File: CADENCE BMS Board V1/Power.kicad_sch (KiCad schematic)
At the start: 62 parts, among them J20 Conn_01x02, J28 Banana Socket PWR, J29 Banana Socket VSS, U1 TVS2200DRV, U2 LT8612, U3 LT3652IMSE#PBF

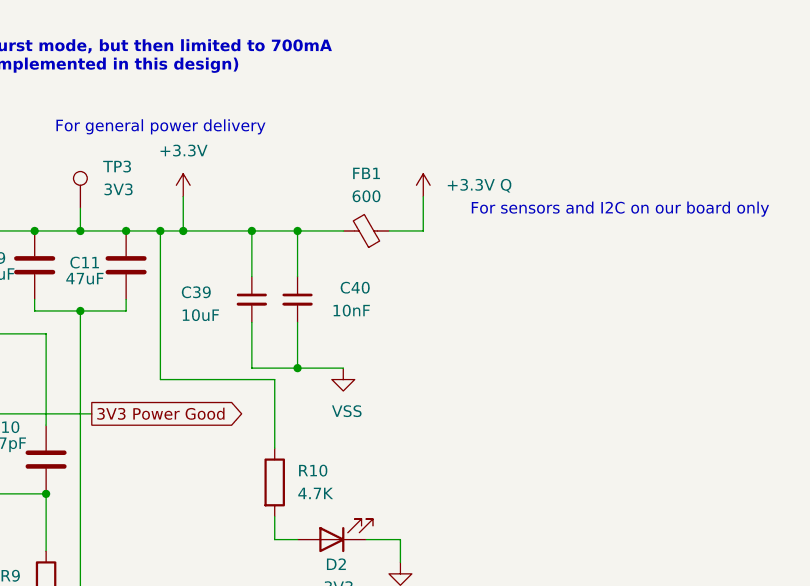
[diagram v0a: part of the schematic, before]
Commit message: Removed 3v3Q
Removed 3v3Q, Capacitors (EMI FILTER OUT), Changed all +3.3V Q -> 3.3V
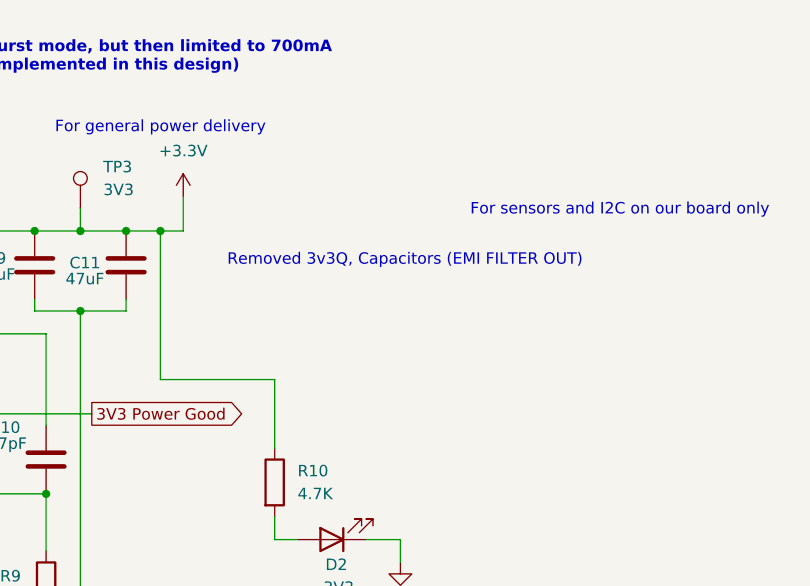
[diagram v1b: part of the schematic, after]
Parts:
- removed C39: 10uF, Capacitor_SMD:C_1210_3225Metric, symbol Device:C_Small
- removed C40: 10nF, Capacitor_SMD:C_0805_2012Metric, symbol Device:C_Small
- removed FB1: 600, Inductor_SMD:L_1008_2520Metric, symbol Device:FerriteBead_Small
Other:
- note added: "Removed 3v3Q, Capacitors (EMI FILTER OUT)"

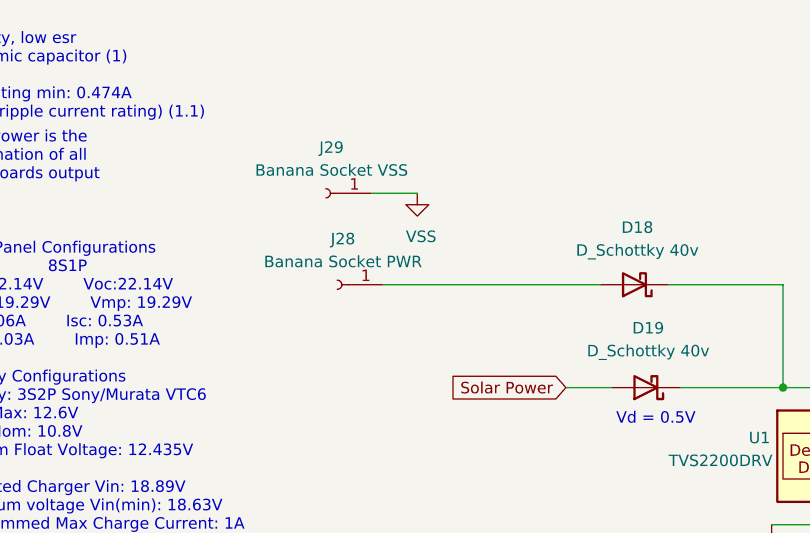
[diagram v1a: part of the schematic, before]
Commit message: Updates for USB-C charging and set up for testing
Revamped USB-C layout to make it cleaner and more compressed and also included schematic parts for adding in Banana plugs for testing the PCB
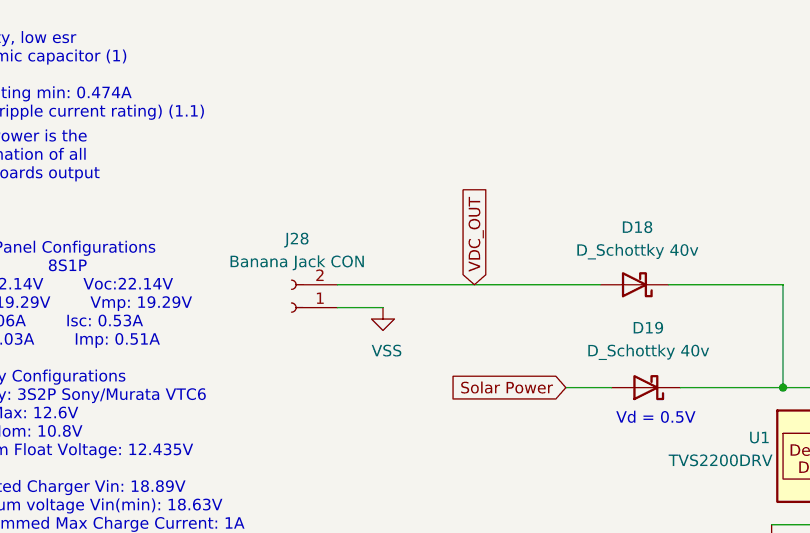
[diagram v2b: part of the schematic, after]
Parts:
- removed J28: Banana Socket PWR, Connector:Banana_Cliff_FCR7350R_S16N-PC_Horizontal, symbol Connector:Conn_01x01_Socket
- removed J29: Banana Socket VSS, Connector:Banana_Cliff_FCR7350B_S16N-PC_Horizontal, symbol Connector:Conn_01x01_Socket
- added J28: Banana Jack CON, Connector:Banana_Jack_2Pin, symbol Connector:Conn_01x02_Socket
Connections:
- net VSS: now also J28.1 (Pin_1)
- net VDC_OUT: now reaches D18.2 (A)
- net VDC_OUT: now also J28.2 (Pin_2)
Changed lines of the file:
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@@
 	(wire
 		(pts
-			(xy 78.74 46.99) (xy 102.87 46.99)
-		)
-		(stroke
-			(width 0)
-			(type default)
-		)
-	)
-	(wire
-		(pts
 			(xy 124.46 331.47) (xy 124.46 337.82)
 		)
@@
 	(wire
 		(pts
-			(xy 77.47 36.83) (xy 82.55 36.83)
+			(xy 73.66 49.53) (xy 78.74 49.53)
 		)
 		(stroke
@@
 	(wire
 		(pts
+			(xy 73.66 46.99) (xy 102.87 46.99)
+		)
+		(stroke
+			(width 0)
+			(type default)
+		)
+	)
+	(wire
+		(pts
 			(xy 341.63 63.5) (xy 346.71 63.5)
 		)
@@
 		)
 	)
+	(global_label "VDC_OUT"
+		(shape input)
+		(at 88.9 46.99 90)
+		(fields_autoplaced yes)
+		(effects
+			(font
+				(size 1.27 1.27)
+			)
+			(justify left)
+		)
+		(property "Intersheetrefs" "${INTERSHEET_REFS}"
+			(at 88.9 35.78 90)
+			(hide yes)
+			(show_name no)
+			(do_not_autoplace no)
+			(effects
+				(font
+					(size 1.27 1.27)
+				)
+				(justify left)
+			)
+		)
+	)
 	(global_label "NTC"
 		(shape input)
@@
 	)
 	(symbol
-		(lib_id "Connector:Conn_01x01_Socket")
-		(at 73.66 46.99 180)
-		(unit 1)
-		(body_style 1)
-		(exclude_from_sim no)
-		(in_bom yes)
-		(on_board yes)
-		(in_pos_files yes)
-		(dnp no)
-		(fields_autoplaced yes)
-		(property "Reference" "J28"
-			(at 74.295 41.91 0)
-			(show_name no)
-			(do_not_autoplace no)
-			(effects
-				(font
-					(size 1.27 1.27)
-				)
-			)
-		)
-		(property "Value" "Banana Socket PWR"
-			(at 74.295 44.45 0)
-			(show_name no)
-			(do_not_autoplace no)
-			(effects
-				(font
-					(size 1.27 1.27)
-				)
-			)
-		)
-		(property "Footprint" "Connector:Banana_Cliff_FCR7350R_S16N-PC_Horizontal"
-			(at 73.66 46.99 0)
-			(hide yes)
-			(show_name no)
-			(do_not_autoplace no)
-			(effects
-				(font
-					(size 1.27 1.27)
-				)
-			)
-		)
-		(property "Datasheet" ""
-			(at 73.66 46.99 0)
-			(hide yes)
-			(show_name no)
-			(do_not_autoplace no)
-			(effects
-				(font
-					(size 1.27 1.27)
-				)
-			)
-		)
-		(property "Description" "Generic connector, single row, 01x01, script generated"
-			(at 73.66 46.99 0)
-			(hide yes)
-			(show_name no)
-			(do_not_autoplace no)
-			(effects
-				(font
-					(size 1.27 1.27)
-				)
-			)
-		)
-		(pin "1"
-		)
-		(instances
-			(project "BMS_Board_Prototype"
-				(path "/4ee99911-836b-4752-8a2d-327c8b28dc47/f4fcff51-0cdb-4e70-aba0-d567fd3e6a03"
-					(reference "J28")
-					(unit 1)
-				)
-			)
-		)
-	)
-	(symbol
 		(lib_id "Device:C")
 		(at 341.63 71.12 0)
@@
 	(symbol
 		(lib_id "power:GND")
-		(at 82.55 36.83 0)
+		(at 78.74 49.53 0)
 		(unit 1)
 		(body_style 1)
@@
 		(dnp no)
 		(property "Reference" "#PWR033"
-			(at 82.55 43.18 0)
+			(at 78.74 55.88 0)
 			(hide yes)
 			(show_name no)
@@
 		)
 		(property "Value" "VSS"
-			(at 81.28 41.656 0)
+			(at 77.47 54.356 0)
 			(show_name no)
 			(do_not_autoplace no)
@@
 		)
 		(property "Footprint" ""
-			(at 82.55 36.83 0)
+			(at 78.74 49.53 0)
 			(hide yes)
 			(show_name no)
@@
 		)
 		(property "Datasheet" ""
-			(at 82.55 36.83 0)
+			(at 78.74 49.53 0)
 			(hide yes)
 			(show_name no)
@@
 		)
 		(property "Description" "Power symbol creates a global label with name \"GND\" , ground"
-			(at 82.55 36.83 0)
+			(at 78.74 49.53 0)
 			(hide yes)
 			(show_name no)
@@
 	)
 	(symbol
+		(lib_id "Connector:Conn_01x02_Socket")
+		(at 68.58 49.53 180)
+		(unit 1)
+		(body_style 1)
+		(exclude_from_sim no)
+		(in_bom yes)
+		(on_board yes)
+		(in_pos_files yes)
+		(dnp no)
+		(fields_autoplaced yes)
+		(property "Reference" "J28"
+			(at 69.215 41.91 0)
+			(show_name no)
+			(do_not_autoplace no)
+			(effects
+				(font
+					(size 1.27 1.27)
+				)
+			)
+		)
+		(property "Value" "Banana Jack CON"
+			(at 69.215 44.45 0)
+			(show_name no)
+			(do_not_autoplace no)
+			(effects
+				(font
+					(size 1.27 1.27)
+				)
+			)
+		)
+		(property "Footprint" "Connector:Banana_Jack_2Pin"
+			(at 68.58 49.53 0)
+			(hide yes)
+			(show_name no)
+			(do_not_autoplace no)
+			(effects
+				(font
+					(size 1.27 1.27)
+				)
+			)
+		)
+		(property "Datasheet" ""
+			(at 68.58 49.53 0)
+			(hide yes)
+			(show_name no)
+			(do_not_autoplace no)
+			(effects
+				(font
+					(size 1.27 1.27)
+				)
+			)
+		)
+		(property "Description" "Generic connector, single row, 01x02, script generated"
+			(at 68.58 49.53 0)
+			(hide yes)
+			(show_name no)
+			(do_not_autoplace no)
+			(effects
+				(font
+					(size 1.27 1.27)
+				)
+			)
+		)
+		(pin "1"
+		)
+		(pin "2"
+		)
+		(instances
+			(project "BMS_Board_Prototype"
+				(path "/4ee99911-836b-4752-8a2d-327c8b28dc47/f4fcff51-0cdb-4e70-aba0-d567fd3e6a03"
+					(reference "J28")
+					(unit 1)
+				)
+			)
+		)
+	)
+	(symbol
 		(lib_id "power:GND")
 		(at 88.9 327.66 0)
@@
 					(unit 1)
 				)
-			)
-		)
-	)
-	(symbol
-		(lib_id "Connector:Conn_01x01_Socket")
-		(at 72.39 36.83 180)
-		(unit 1)
-		(body_style 1)
-		(exclude_from_sim no)
-		(in_bom yes)
-		(on_board yes)
-		(in_pos_files yes)
-		(dnp no)
-		(fields_autoplaced yes)
-		(property "Reference" "J29"
-			(at 73.025 31.75 0)
-			(show_name no)
-			(do_not_autoplace no)
-			(effects
-				(font
-					(size 1.27 1.27)
-				)
-			)
-		)
-		(property "Value" "Banana Socket VSS"
-			(at 73.025 34.29 0)
-			(show_name no)
-			(do_not_autoplace no)
-			(effects
-				(font
-					(size 1.27 1.27)
-				)
-			)
-		)
-		(property "Footprint" "Connector:Banana_Cliff_FCR7350B_S16N-PC_Horizontal"
-			(at 72.39 36.83 0)
-			(hide yes)
-			(show_name no)
-			(do_not_autoplace no)
-			(effects
-				(font
-					(size 1.27 1.27)
-				)
-			)
-		)
-		(property "Datasheet" ""
-			(at 72.39 36.83 0)
-			(hide yes)
-			(show_name no)
-			(do_not_autoplace no)
-			(effects
-				(font
-					(size 1.27 1.27)
-				)
-			)
-		)
-		(property "Description" "Generic connector, single row, 01x01, script generated"
-			(at 72.39 36.83 0)
-			(hide yes)
-			(show_name no)
-			(do_not_autoplace no)
-			(effects
-				(font
-					(size 1.27 1.27)
-				)
-			)
-		)
-		(pin "1"
-		)
-		(instances
-			(project "BMS_Board_Prototype"
-				(path "/4ee99911-836b-4752-8a2d-327c8b28dc47/f4fcff51-0cdb-4e70-aba0-d567fd3e6a03"
-					(reference "J29")
-					(unit 1)
-				)

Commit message: New connectors and adding in a test setup
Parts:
- removed J28: Banana Jack CON, Connector:Banana_Jack_2Pin, symbol Connector:Conn_01x02_Socket
- added D20, D21: D_Schottky 40v, Diode_SMD:D_SMA, symbol Device:D_Schottky
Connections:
- net Cell 1+: no longer C41.1, L5.1, TP1.1
- net VDC_OUT: now also D20.2 (A); no longer D18.2 (A)
- net at C4.1, C5.1, D18.1 (K)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: now also D20.1 (K), D21.1 (K)
- net V_mppt_o: now reaches C7.1, R3.1, TP2.1, U3.1 (VIN)
- net V_mppt_o: no longer C6.1, R2.2
- new net TEST_PWR: D18.2 (A)
- new net UNREG: C41.1, L5.1, TP1.1
- new net USB PWR: D21.2 (A)
- new net V_mppt_i: C6.1, R2.2
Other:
- moved on the sheet: D18

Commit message: Updates to incorporate inhibit board
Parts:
- removed C14: 10nF, Capacitor_SMD:C_0805_2012Metric, symbol Device:C
- removed C15: 10uF, Capacitor_SMD:C_1210_3225Metric, symbol Device:C
- removed C16: 4.7uF, Capacitor_SMD:C_1206_3216Metric, symbol Device:C
- removed L4: 4.7u, FNR5040S4R7MT:FNR5040S4R7MT, symbol Device:L
- R12, R49, R50: footprint Resistor_SMD:R_2512_6332Metric -> Resistor_SMD:R_0603_1608Metric
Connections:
- net Cell 1+: now also C13.1, D3.1 (K), R12.1, R14.2, U3.9 (BAT)
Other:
- moved on the sheet: D19, D6, R15, TP4

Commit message: More documentation on Fault signal Voltages
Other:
- note added: "The voltage for CHG' and FAULT' are .4V"
- note added: "The voltage for SHDN' is 1.2V nom with (+/-) .5V"

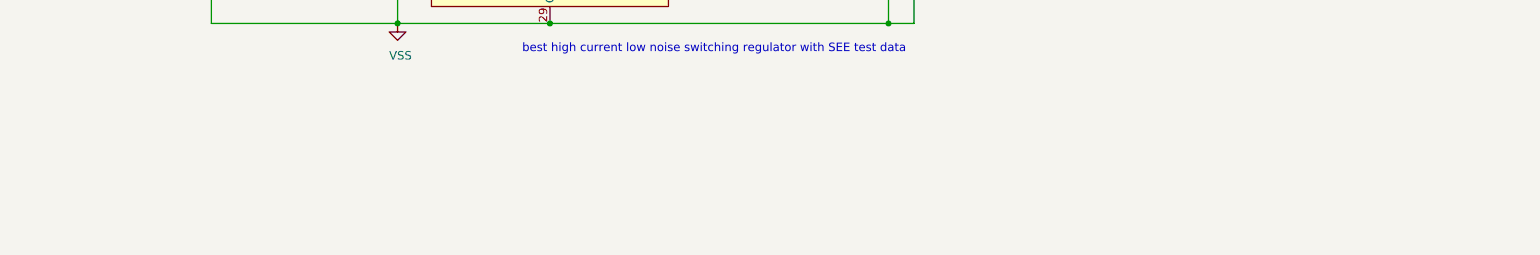
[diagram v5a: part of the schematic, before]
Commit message: Updated for an error found with Power good alert
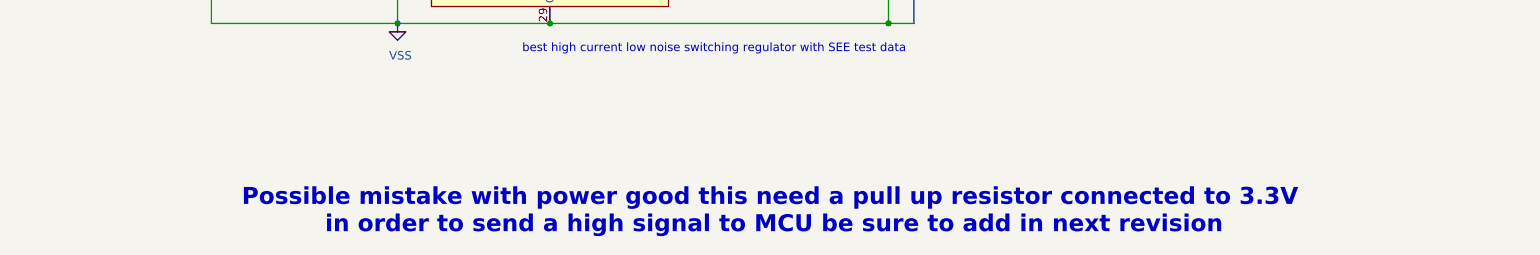
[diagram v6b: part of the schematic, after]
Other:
- note added: "Possible mistake with power good this need a pull up resistor connected to 3.3V in order to send a high signal to MCU be sure to add in next revision"
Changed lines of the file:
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@@
+		)
+	)
+	(text "Possible mistake with power good this need a pull up resistor connected to 3.3V\n in order to send a high signal to MCU be sure to add in next revision\n"
+		(exclude_from_sim no)
+		(at 201.93 397.764 0)
+		(effects
+			(font
+				(size 2.54 2.54)
+				(thickness 0.508)
+				(bold yes)
+			)
 		)
 	)
